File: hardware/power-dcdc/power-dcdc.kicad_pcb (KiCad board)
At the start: 2 copper layers, 110 x 70 mm, 117 parts, among them J1 SOLAR_IN, J2 BATT2, J3 BATT1, J4 Conn_01x05_Male, J5 CANPWR, J6 CANGND, J7 RJ45, J8 RJ45, J9 Conn_02x03_Odd_Even, Q1 SIR164ADP, Q2 SIR164ADP, Q3 SI7149ADP, Q4 SI7149ADP, Q5 SI7149ADP, Q6 SI7149ADP, Q7 BSS123, SW1 next, SW2 select, U1 AP63200WU, U2 LP4951C, U3 NCP5901B, U4 PAC1953-1, U5 DGD0215, U6 DGD0215, U7 2.048V, U8 PIC18F27Q84, U9 TLE9250VSJXUMA1, Y1 10Mhz

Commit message: Split project in 2 boards: the power DC/DC and associated instrumentation, and control (with pic18 and canbus)
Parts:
- removed the C1 at (317.6, 177.0)
- removed the C2 at (317.6, 180.2)
- removed C27, C30, C31, C32: 100nF, Capacitor_SMD:C_0805_2012Metric_Pad1.18x1.45mm_HandSolder
- removed C28, C29: 22pF, Capacitor_THT:C_Disc_D3.8mm_W2.6mm_P2.50mm
- removed the C3 at (317.6, 173.9)
- removed C33: 100nF, local:C_filter_0805
- removed the C4 at (320.0, 166.1)
- removed the C5 at (316.4, 163.7)
- removed the C6 at (341.4, 172.2)
- removed the C7 at (337.8, 172.2)
- removed the D1 at (331.4, 79.0)
- removed the D2 at (337.1, 79.0)
- removed D6: SMBJ16A, Diode_SMD:D_SMB_Handsoldering
- removed DI1: MCOB128064JX, LCDdisplays.mod:MCOB128064JX
- removed the F1 at (309.8, 73.7)
- removed the F2 at (385.9, 47.4)
- removed J4: Conn_01x05_Male, Connector_PinHeader_2.54mm:PinHeader_1x05_P2.54mm_Vertical
- removed J5: CANPWR, Connector_PinHeader_2.54mm:PinHeader_1x02_P2.54mm_Vertical
- removed J6: CANGND, Connector_PinHeader_2.54mm:PinHeader_1x02_P2.54mm_Vertical
- removed J7, J8: RJ45, Connector_RJ:RJ45_Amphenol_54602-x08_Horizontal
- removed J9: Conn_02x03_Odd_Even, Connector_PinHeader_2.54mm:PinHeader_2x03_P2.54mm_Vertical
- removed the L1 at (328.7, 170.7)
- removed Q7: BSS123, Package_TO_SOT_SMD:SOT-23
- removed the R1 at (312.5, 171.7)
- removed the R2 at (312.5, 167.1)
- removed R23, R24, R25, R26, R27, R28, R31: 10K, Resistor_SMD:R_0805_2012Metric_Pad1.20x1.40mm_HandSolder
- removed R29, R30: 4K7, Resistor_SMD:R_0805_2012Metric_Pad1.20x1.40mm_HandSolder
- removed the R3 at (316.4, 166.9)
- removed R32: 100K, Resistor_SMD:R_0805_2012Metric_Pad1.20x1.40mm_HandSolder
- removed R33: 100, Resistor_SMD:R_0805_2012Metric_Pad1.20x1.40mm_HandSolder
- removed the R4 at (311.4, 163.1)
- removed the R5 at (353.1, 141.7)
- removed the R6 at (383.0, 52.4)
- removed the R7 at (411.6, 17.8)
- removed SW1: next, Button_Switch_THT:Push_E-Switch_KS01Q01
- removed SW2: select, Button_Switch_THT:Push_E-Switch_KS01Q01
- removed TH1: NTC10K, Resistor_SMD:R_0201_0603Metric_Pad0.64x0.40mm_HandSolder
- removed the U1 at (317.6, 170.7)
- removed U7: 2.048V, Package_TO_SOT_SMD:SOT-23
- removed U8: PIC18F27Q84, Package_SO:SOIC-28W_7.5x17.9mm_P1.27mm
- removed U9: TLE9250VSJXUMA1, Package_SO:SOIC-8_3.9x4.9mm_P1.27mm
- removed Y1: 10Mhz, Crystal:Crystal_HC18-U_Vertical
- moved H2 100.0 mm to (155.0, 85.0)
- moved H3 100.0 mm to (55.0, 145.0)
- moved H1 60.0 mm to (55.0, 85.0)
- moved H4 60.0 mm to (155.0, 145.0)
- renumbered C8 to C1, C17 to C10, C18 to C11, C19 to C12, C20 to C13, C21 to C14, C22 to C15, C23 to C16, C24 to C17, C25 to C18, C26 to C19, C9 to C2, C10 to C3, C11 to C4, C12 to C5, C13 to C6, C14 to C7, C15 to C8, C16 to C9, D3 to D1, D4 to D2, D5 to D3, F3 to F1, F4 to F2, F5 to F3, F6 to F4, F7 to F5, F8 to F6, F9 to F7, L2 to L1, R8 to R1, R17 to R10, R18 to R11, R19 to R12, R20 to R13, R21 to R14, R22 to R15, R9 to R2, R10 to R3, R11 to R4, R12 to R5, R13 to R6, R14 to R7, R15 to R8, R16 to R9, U2 to U1, U3 to U2, U4 to U3, U5 to U4, U6 to U5
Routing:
- net +5V: track 47.2 -> 9.38 mm
- net GND: track 50.1 -> 13.7 mm
- net Net-(C1-Pad1): track 13.3 -> 0.00 mm
- net Net-(C4-Pad1): track 13.3 -> 0.00 mm
- net Net-(C5-Pad2): track 9.70 -> 0.00 mm
- net Net-(R1-Pad2): track 6.54 -> 0.00 mm
- net Net-(C4-Pad2): track 3.11 -> 0.00 mm

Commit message: Rsync PCB with schematic
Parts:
- C19, R14, R15: moved to B.Cu
- moved C2 294.3 mm to (57.0, 126.2), turned to 90 degrees
- moved C19 245.5 mm to (142.6, 96.0), turned to 180 degrees
- moved R15 216.8 mm to (142.6, 99.9)
- moved R14 215.5 mm to (137.2, 99.9)
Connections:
- net /DC-DC/+7V renamed /+7V
- net /DC-DC/AL1 renamed /AL1
- net /DC-DC/AL2 renamed /AL2
- net /DC-DC/BATT1+ renamed /BATT1+
- net /DC-DC/BATT1_ON renamed BATT1_ON
- net /DC-DC/BATT2+ renamed /BATT2+
- net /DC-DC/BATT2_ON renamed BATT2_ON
- net /DC-DC/PWM renamed /PWM
- net /DC-DC/PWM_OFF renamed /PWM_OFF
- net /DC-DC/PWM_OK renamed /PWM_OK
- net /DC-DC/PWM_V renamed PWM_V
- net /DC-DC/SCL renamed /SCL
- net /DC-DC/SDA renamed /SDA
- net /DC-DC/SOLAR+ renamed /SOLAR+
- net /DC-DC/SOLAR_PWR renamed /SOLAR_PWR
- net /DC-DC/~{PAC_DOWN} renamed /~{PAC_DOWN}
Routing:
- net PWM_V: track 0.00 -> 7.41 mm

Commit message: Finish routing the power board
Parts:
- added J4: DCDC-MEASURES, Connector_PinSocket_2.54mm:PinSocket_2x05_P2.54mm_Vertical, F.Cu at (150.0, 95.0)
- added J5: DCDC-PWM, Connector_PinSocket_2.54mm:PinSocket_2x05_P2.54mm_Vertical, F.Cu at (65.0, 85.0)
- R1, R5: value 56K -> 100K; footprint Resistor_SMD:R_1206_3216Metric_Pad1.30x1.75mm_HandSolder -> Resistor_THT:R_Axial_DIN0309_L9.0mm_D3.2mm_P12.70mm_Horizontal
- R7, R9: footprint Resistor_SMD:R_0805_2012Metric_Pad1.20x1.40mm_HandSolder -> Resistor_THT:R_Axial_DIN0309_L9.0mm_D3.2mm_P12.70mm_Horizontal
- moved R1 308.5 mm to (72.8, 82.9), turned to -90 degrees
- moved R5 264.1 mm to (69.0, 82.9), turned to -90 degrees
- moved R7 39.2 mm to (135.3, 87.2), turned to 0 degrees
- moved R9 34.5 mm to (135.3, 91.1), turned to 0 degrees
- moved R8 33.7 mm to (141.1, 94.7), turned to 0 degrees
- moved R15 22.2 mm to (123.6, 88.5), turned to -90 degrees
- moved C19 17.4 mm to (126.9, 88.5), turned to 90 degrees
- moved R14 9.42 mm to (129.7, 94.2), turned to 90 degrees
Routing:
- net BATT2_ON: track 0.00 -> 201.5 mm, vias 0 -> 2
- net BATT1_ON: track 0.00 -> 143.7 mm, vias 0 -> 2
- net +5V: track 9.38 -> 141.5 mm, vias 0 -> 1
- net /SDA: track 0.00 -> 105.8 mm, vias 0 -> 1
- net /SCL: track 0.00 -> 105.0 mm, vias 0 -> 1
- net /PWM_OFF: track 0.00 -> 80.5 mm
- net /AL1: track 3.23 -> 82.3 mm
- net /~{PAC_DOWN}: track 9.19 -> 78.4 mm, vias 0 -> 1
- net /AL2: track 5.53 -> 72.5 mm
- net /PWM_OK: track 10.3 -> 73.6 mm
- net PWM_V: track 7.41 -> 69.2 mm
- net /PWM: track 0.00 -> 34.5 mm, vias 0 -> 1
- net /SOLAR_PWR: track 35.9 -> 48.8 mm
- net GND: vias 12 -> 15

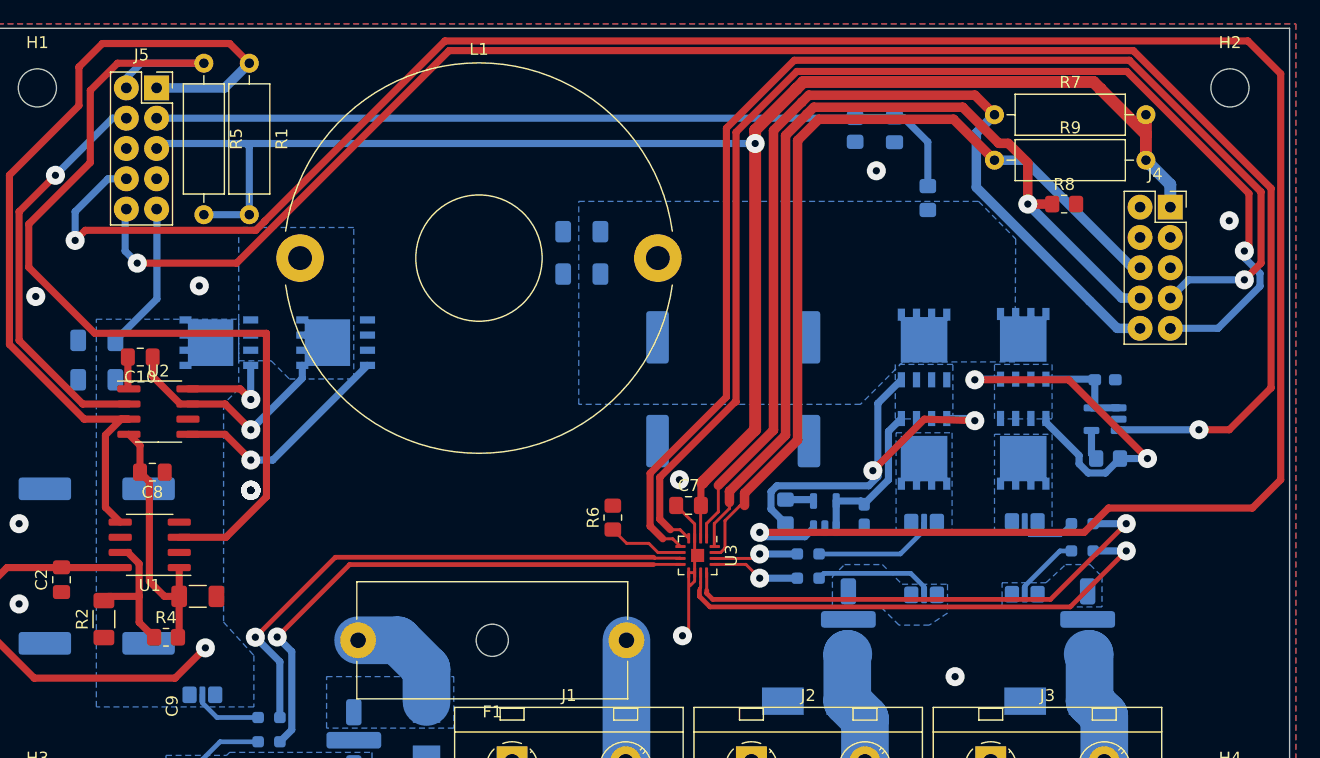
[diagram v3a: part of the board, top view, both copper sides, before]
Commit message: Make sure to remove isolated ground planes. Add more GND vias.
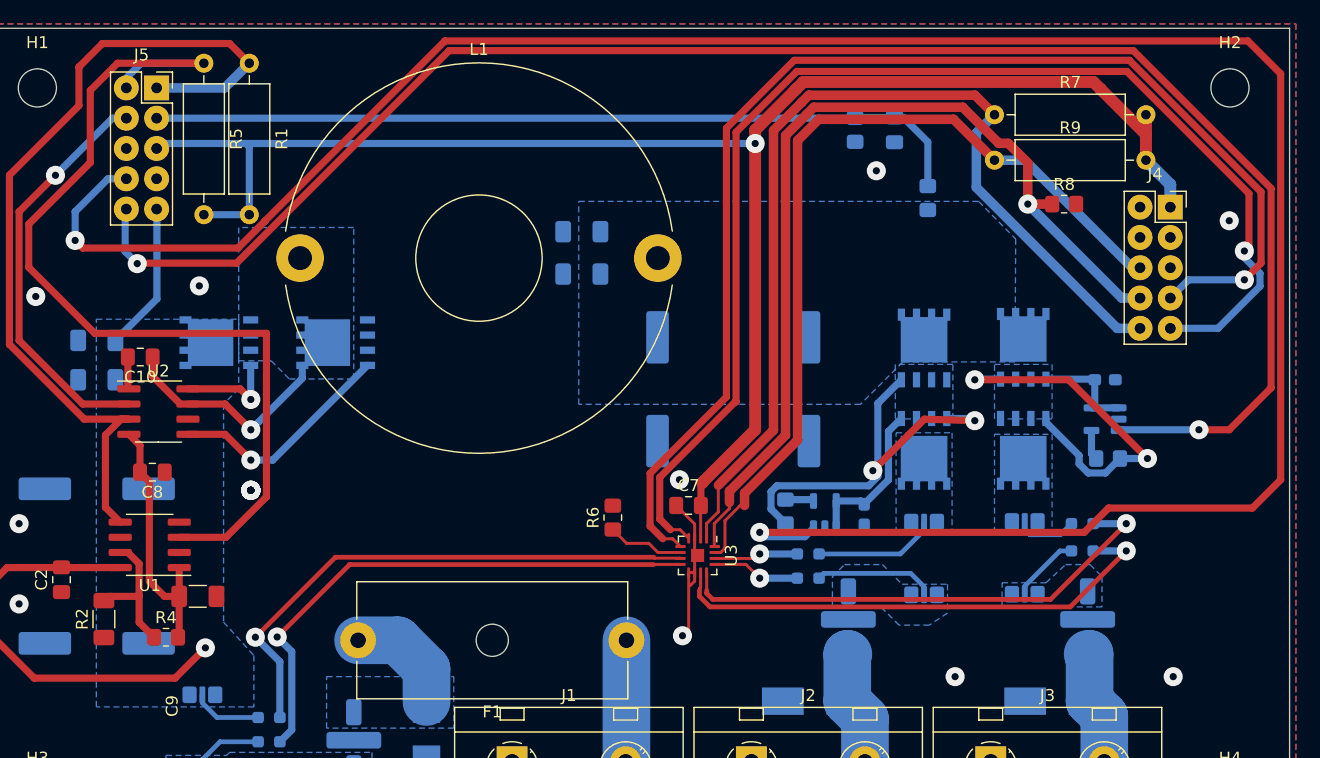
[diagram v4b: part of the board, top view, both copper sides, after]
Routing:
- net BATT2_ON: track 201.5 -> 202.1 mm
- net GND: vias 15 -> 16
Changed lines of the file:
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@@
   (via (at 53.467 128.27) (size 1.6) (drill 0.6) (layers "F.Cu" "B.Cu") (free) (net 2))
   (via (at 72.898 118.745) (size 1.6) (drill 0.6) (layers "F.Cu" "B.Cu") (free) (net 2))
+  (via (at 150.241 134.366) (size 1.6) (drill 0.6) (layers "F.Cu" "B.Cu") (free) (net 2))
   (via (at 72.898 118.745) (size 1.6) (drill 0.6) (layers "F.Cu" "B.Cu") (free) (net 2))
   (via (at 125.349 91.948) (size 1.6) (drill 0.6) (layers "F.Cu" "B.Cu") (free) (net 2))
@@
   (segment (start 144.57 117.288) (end 145.78 116.078) (width 0.6) (layer "B.Cu") (net 42))
   (segment (start 142.349 116.521802) (end 143.115198 117.288) (width 0.6) (layer "B.Cu") (net 42))
+  (segment (start 89.178198 81.063494) (end 74.081 96.160692) (width 0.6) (layer "F.Cu") (net 44))
+  (segment (start 74.081 96.17362) (end 71.82962 98.425) (width 0.6) (layer "F.Cu") (net 44))
+  (segment (start 142.779503 122.269497) (end 144.82 120.229) (width 0.6) (layer "F.Cu") (net 44))
+  (segment (start 156.885 120.229) (end 159.258 117.856) (width 0.6) (layer "F.Cu") (net 44))
+  (segment (start 144.82 120.229) (end 156.885 120.229) (width 0.6) (layer "F.Cu") (net 44))
+  (segment (start 74.081 96.160692) (end 74.081 96.17362) (width 0.6) (layer "F.Cu") (net 44))
+  (segment (start 159.258 117.856) (end 159.258 83.82) (width 0.6) (layer "F.Cu") (net 44))
+  (segment (start 115.57 122.269497) (end 142.779503 122.269497) (width 0.6) (layer "F.Cu") (net 44))
   (segment (start 156.501494 81.063494) (end 89.178198 81.063494) (width 0.6) (layer "F.Cu") (net 44))
-  (segment (start 115.57 122.269497) (end 142.779503 122.269497) (width 0.6) (layer "F.Cu") (net 44))
-  (segment (start 89.178198 81.063494) (end 74.081 96.160692) (width 0.6) (layer "F.Cu") (net 44))
-  (segment (start 74.081 96.160692) (end 74.081 96.17362) (width 0.6) (layer "F.Cu") (net 44))
   (segment (start 159.258 83.82) (end 156.501494 81.063494) (width 0.6) (layer "F.Cu") (net 44))
-  (segment (start 144.82 120.229) (end 156.885 120.229) (width 0.6) (layer "F.Cu") (net 44))
-  (segment (start 159.258 117.856) (end 159.258 83.82) (width 0.6) (layer "F.Cu") (net 44))
-  (segment (start 156.885 120.229) (end 159.258 117.856) (width 0.6) (layer "F.Cu") (net 44))
-  (segment (start 142.779503 122.269497) (end 144.82 120.229) (width 0.6) (layer "F.Cu") (net 44))
-  (segment (start 73.31362 96.941) (end 59.015 96.941) (width 0.6) (layer "F.Cu") (net 44))
-  (segment (start 59.015 96.941) (end 58.166 97.79) (width 0.6) (layer "F.Cu") (net 44))
-  (segment (start 74.081 96.17362) (end 73.31362 96.941) (width 0.6) (layer "F.Cu") (net 44))
+  (segment (start 71.82962 98.425) (end 58.801 98.425) (width 0.6) (layer "F.Cu") (net 44))
+  (segment (start 58.801 98.425) (end 58.166 97.79) (width 0.6) (layer "F.Cu") (net 44))
   (via (at 58.166 97.79) (size 1.6) (drill 0.6) (layers "F.Cu" "B.Cu") (net 44))
   (via (at 115.57 122.269497) (size 1.6) (drill 0.6) (layers "F.Cu" "B.Cu") (net 44))
@@
   (segment (start 119.3625 122.633) (end 120.081 121.9145) (width 0.6) (layer "B.Cu") (net 44))
   (segment (start 58.166 95.377) (end 60.923 92.62) (width 0.6) (layer "B.Cu") (net 44))
-  (segment (start 89.526432 81.872995) (end 146.900609 81.872994) (width 0.6) (layer "F.Cu") (net 45))
-  (segment (start 71.704427 99.695) (end 89.526432 81.872995) (width 0.6) (layer "F.Cu") (net 45))
-  (segment (start 154.94 113.665) (end 152.4 113.665) (width 0.6) (layer "F.Cu") (net 45))
-  (segment (start 158.448 110.157) (end 154.94 113.665) (width 0.6) (layer "F.Cu") (net 45))
-  (segment (start 158.448 93.420386) (end 158.448 110.157) (width 0.6) (layer "F.Cu") (net 45))
-  (segment (start 63.373 99.695) (end 71.704427 99.695) (width 0.6) (layer "F.Cu") (net 45))
-  (segment (start 146.900609 81.872994) (end 158.448 93.420386) (width 0.6) (layer "F.Cu") (net 45))
+  (segment (start 146.900609 81.872994) (end 89.526432 81.872995) (width 0.6) (layer "F.Cu") (net 45))
+  (segment (start 152.4 113.665) (end 154.94 113.665) (width 0.6) (layer "F.Cu") (net 45))
+  (segment (start 89.526432 81.872995) (end 71.704427 99.695) (width 0.6) (layer "F.Cu") (net 45))
+  (segment (start 154.94 113.665) (end 158.448 110.157) (width 0.6) (layer "F.Cu") (net 45))
+  (segment (start 71.704427 99.695) (end 63.4125 99.695) (width 0.6) (layer "F.Cu") (net 45))
+  (segment (start 158.448 110.157) (end 158.448 93.420386) (width 0.6) (layer "F.Cu") (net 45))
+  (segment (start 63.4125 99.695) (end 63.373 99.7345) (width 0.6) (layer "F.Cu") (net 45))
+  (segment (start 158.448 93.420386) (end 146.900609 81.872994) (width 0.6) (layer "F.Cu") (net 45))
   (via (at 152.4 113.665) (size 1.6) (drill 0.6) (layers "F.Cu" "B.Cu") (net 45))
-  (via (at 63.373 99.695) (size 1.6) (drill 0.6) (layers "F.Cu" "B.Cu") (net 45))
+  (via (at 63.373 99.7345) (size 1.6) (drill 0.6) (layers "F.Cu" "B.Cu") (net 45))
   (segment (start 145.7245 113.665) (end 145.6635 113.726) (width 0.6) (layer "B.Cu") (net 45))
+  (segment (start 152.4 113.665) (end 145.7245 113.665) (width 0.6) (layer "B.Cu") (net 45))
+  (segment (start 62.357 98.7185) (end 63.373 99.7345) (width 0.6) (layer "B.Cu") (net 45))
+  (segment (start 62.357 95.016) (end 62.357 98.7185) (width 0.6) (layer "B.Cu") (net 45))
   (segment (start 62.631 94.742) (end 62.357 95.016) (width 0.6) (layer "B.Cu") (net 45))
-  (segment (start 152.4 113.665) (end 145.7245 113.665) (width 0.6) (layer "B.Cu") (net 45))
-  (segment (start 62.357 98.679) (end 63.373 99.695) (width 0.6) (layer "B.Cu") (net 45))
-  (segment (start 62.357 95.016) (end 62.357 98.679) (width 0.6) (layer "B.Cu") (net 45))
   (segment (start 52.657 92.3135) (end 52.657 106.507512) (width 0.6) (layer "F.Cu") (net 46))
   (segment (start 60.452 81.28) (end 58.4835 83.2485) (width 0.6) (layer "F.Cu") (net 46))
@@
     (connect_pads (clearance 0.21))
     (min_thickness 0.254) (filled_areas_thickness no)
-    (fill yes (thermal_gap 0.508) (thermal_bridge_width 0.508) (smoothing fillet) (radius 1) (island_removal_mode 1) (island_area_min 0))
+    (fill yes (thermal_gap 0.508) (thermal_bridge_width 0.508) (smoothing fillet) (radius 1))
     (polygon
       (pts

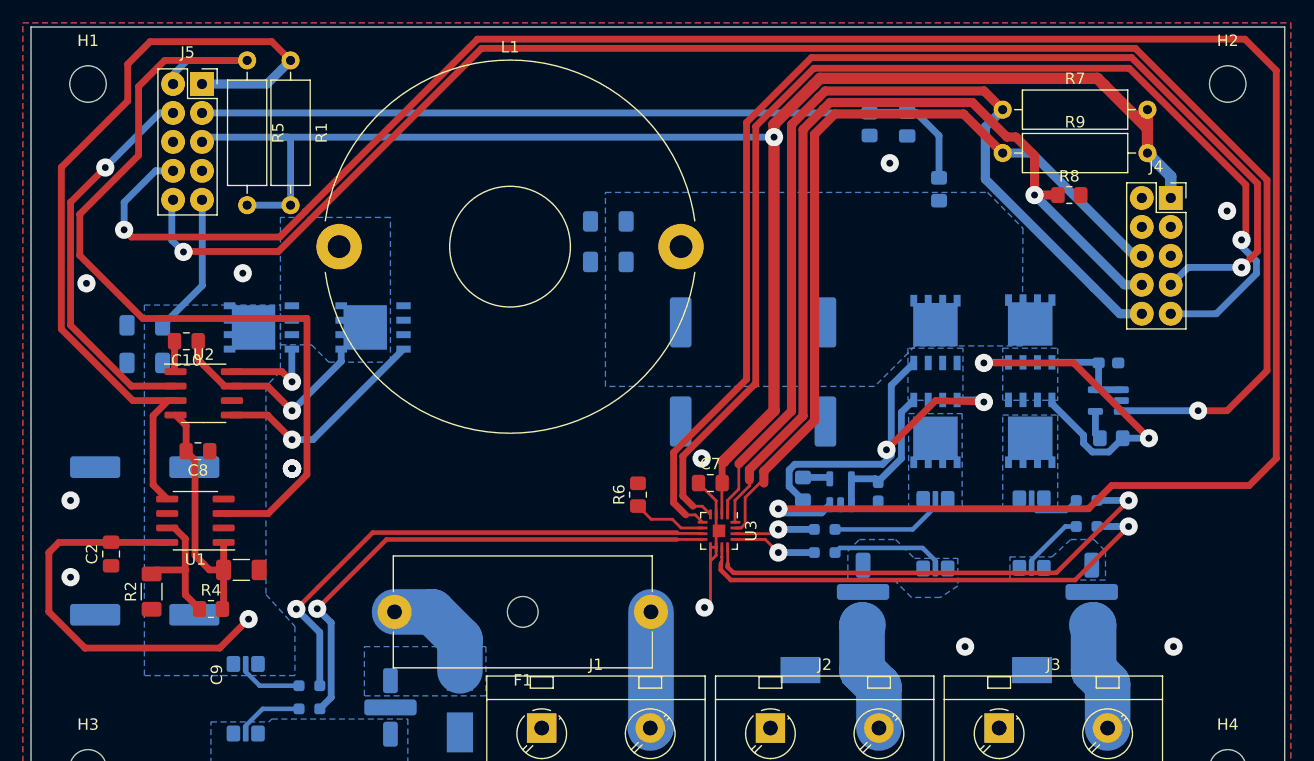
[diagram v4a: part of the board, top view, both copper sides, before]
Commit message: Move thermistor to power-dcdc board (measure board temp) Adjust power-dcdc board layout, pass DRC
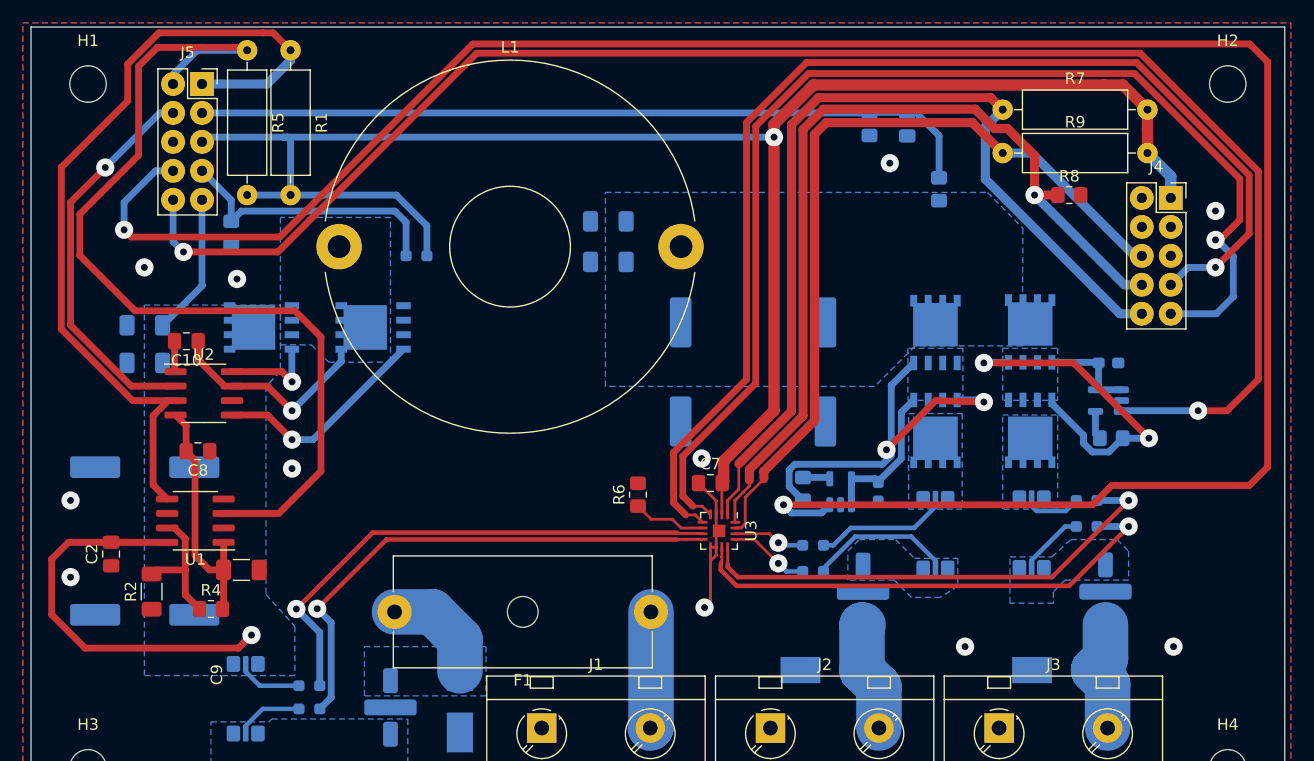
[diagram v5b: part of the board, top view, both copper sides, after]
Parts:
- added R16: 10K, Resistor_SMD:R_0805_2012Metric_Pad1.20x1.40mm_HandSolder, B.Cu at (67.6, 98.0)
- added TH1: NTC10K, Resistor_SMD:R_0603_1608Metric_Pad0.98x0.95mm_HandSolder, B.Cu at (83.8, 100.1)
- moved F5 1.94 mm to (118.6, 127.8)
- moved F4 1.73 mm to (118.6, 125.5)
- moved C16 1.20 mm to (144.3, 129.5)
- moved R1 0.89 mm to (72.8, 82.0)
- moved R5 0.89 mm to (69.0, 82.0)
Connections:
- J5 pad 6: unconnected-(J5-Pad6) -> GND
- J5 pad 7: GND -> /TH
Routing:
- net /TH: track 0.00 -> 24.5 mm
- net +5V: track 141.5 -> 155.1 mm
- net /PWM_OFF: track 80.5 -> 83.8 mm
- net Net-(F5-Pad1): track 10.1 -> 12.8 mm
- net /SDA: track 105.8 -> 103.5 mm
- net BATT2_ON: track 202.1 -> 200.2 mm
- net Net-(F4-Pad1): track 10.3 -> 11.9 mm
- net BATT1_ON: track 143.8 -> 142.2 mm
- net /SOLAR_PWR: track 48.8 -> 47.3 mm
- net /AL2: track 72.5 -> 71.7 mm
- net Net-(F4-Pad2): track 7.08 -> 6.33 mm
- net /PWM_OK: track 73.6 -> 74.2 mm
- net GND: vias 16 -> 12
